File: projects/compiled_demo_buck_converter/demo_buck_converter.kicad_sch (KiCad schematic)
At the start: 7 parts, among them U1 LM2596-5

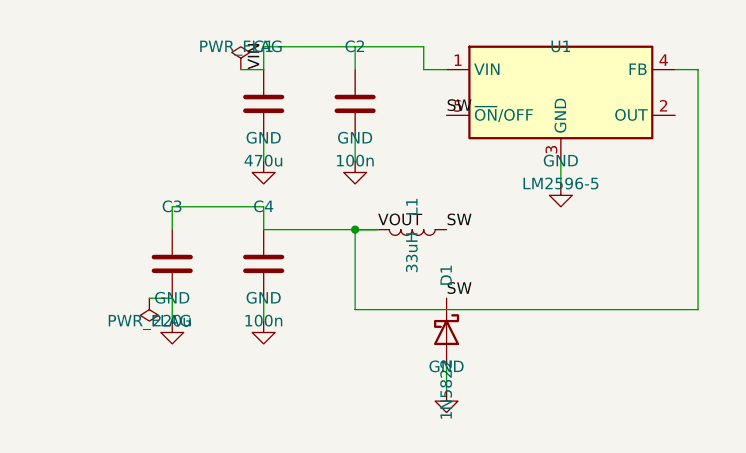
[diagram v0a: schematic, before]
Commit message: F3d+F3e: multi-unit parts and the textplace field autoplacer
Multi-unit: one Symbol per unit (shared ref+lib, distinct unit); nets and
anchors qualify pins as "REF.unit.pin". Resolver targets a specific placed
unit; the geometry probe instantiates per unit. NE5532 (units A/B/C)
compiles first try with both feedback loops wired.

textplace (internal/place2/textplace): deterministic text autoplacement run
at the end of compilation — every visible Reference/Value block is re-placed
horizontally at the least-overlapping side of its body, colliding net labels
flip around their anchor. Fixes the text-collision family the user flagged
on the buck render. KiCad gotcha baked into the pass: a field's drawn angle
is field+symbol rotation, so fields on 90/270 symbols carry a compensating
90 to display horizontal.

All 7 reference circuits now compile from declarative sources with clean
text. Gate demotions (buck SW, ne555 THR/DISCH) are by-design label
fallbacks, zero geometry violations everywhere.

Co-Authored-By: Claude Fable 5 <noreply@anthropic.com>
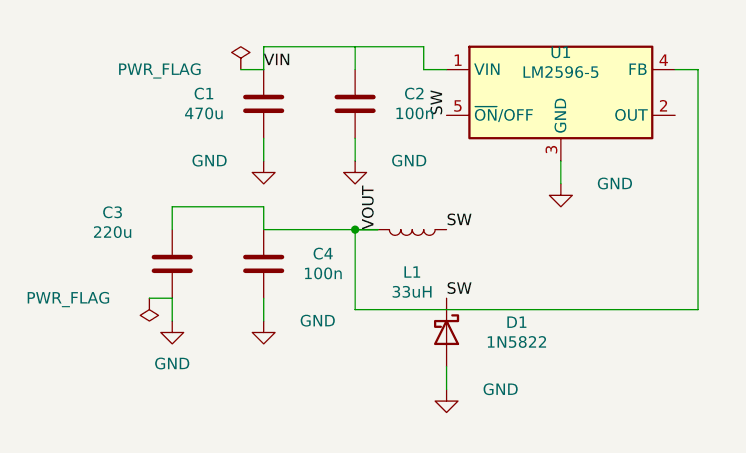
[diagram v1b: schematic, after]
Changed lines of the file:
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@@
     (at 71.12 27.94 0) (unit 1) (exclude_from_sim no) (in_bom yes) (on_board yes) (dnp no)
     (property "Reference" "U1"
-      (at 71.12 22.86 0)
+      (at 71.12 23.52 0)
       (effects
         (font (size 1.27 1.27))))
     (property "Value" "LM2596-5"
-      (at 71.12 38.1 0)
+      (at 71.12 25.72 0)
       (effects
         (font (size 1.27 1.27))))
@@
     (instances
       (project ""
-        (path "/991c5326-0a93-4272-96e1-b9ad8c3713b2" (reference "U1") (unit 1)))))
+        (path "/108c6312-12e9-447c-9139-bc7fdfa02d10" (reference "U1") (unit 1)))))
   (symbol (lib_id "Device:C")
     (at 48.26 29.21 0) (unit 1) (exclude_from_sim no) (in_bom yes) (on_board yes) (dnp no)
     (property "Reference" "C2"
-      (at 48.26 22.86 0)
+      (at 54.87 28.11 0)
       (effects
         (font (size 1.27 1.27))))
     (property "Value" "100n"
-      (at 48.26 35.56 0)
+      (at 54.87 30.31 0)
       (effects
         (font (size 1.27 1.27))))
@@
     (instances
       (project ""
-        (path "/991c5326-0a93-4272-96e1-b9ad8c3713b2" (reference "C2") (unit 1)))))
+        (path "/108c6312-12e9-447c-9139-bc7fdfa02d10" (reference "C2") (unit 1)))))
   (symbol (lib_id "Device:C")
     (at 38.1 29.21 0) (unit 1) (exclude_from_sim no) (in_bom yes) (on_board yes) (dnp no)
     (property "Reference" "C1"
-      (at 38.1 22.86 0)
+      (at 31.49 28.11 0)
       (effects
         (font (size 1.27 1.27))))
     (property "Value" "470u"
-      (at 38.1 35.56 0)
+      (at 31.49 30.31 0)
       (effects
         (font (size 1.27 1.27))))
@@
     (instances
       (project ""
-        (path "/991c5326-0a93-4272-96e1-b9ad8c3713b2" (reference "C1") (unit 1)))))
+        (path "/108c6312-12e9-447c-9139-bc7fdfa02d10" (reference "C1") (unit 1)))))
   (symbol (lib_id "Device:L")
     (at 54.61 43.18 270) (unit 1) (exclude_from_sim no) (in_bom yes) (on_board yes) (dnp no)
     (property "Reference" "L1"
-      (at 54.61 40.64 0)
+      (at 54.61 47.94 90)
       (effects
         (font (size 1.27 1.27))))
     (property "Value" "33uH"
-      (at 54.61 45.72 0)
+      (at 54.61 50.14 90)
       (effects
         (font (size 1.27 1.27))))
@@
     (instances
       (project ""
-        (path "/991c5326-0a93-4272-96e1-b9ad8c3713b2" (reference "L1") (unit 1)))))
+        (path "/108c6312-12e9-447c-9139-bc7fdfa02d10" (reference "L1") (unit 1)))))
   (symbol (lib_id "Diode:1N5822")
     (at 58.42 54.61 270) (unit 1) (exclude_from_sim no) (in_bom yes) (on_board yes) (dnp no)
     (property "Reference" "D1"
-      (at 58.42 48.26 0)
+      (at 66.23 53.51 90)
       (effects
         (font (size 1.27 1.27))))
     (property "Value" "1N5822"
-      (at 58.42 60.96 0)
+      (at 66.23 55.71 90)
       (effects
         (font (size 1.27 1.27))))
@@
     (instances
       (project ""
-        (path "/991c5326-0a93-4272-96e1-b9ad8c3713b2" (reference "D1") (unit 1)))))
+        (path "/108c6312-12e9-447c-9139-bc7fdfa02d10" (reference "D1") (unit 1)))))
   (symbol (lib_id "Device:C")
     (at 38.1 46.99 0) (unit 1) (exclude_from_sim no) (in_bom yes) (on_board yes) (dnp no)
     (property "Reference" "C4"
-      (at 38.1 40.64 0)
+      (at 44.71 45.89 0)
       (effects
         (font (size 1.27 1.27))))
     (property "Value" "100n"
-      (at 38.1 53.34 0)
+      (at 44.71 48.09 0)
       (effects
         (font (size 1.27 1.27))))
@@
     (instances
       (project ""
-        (path "/991c5326-0a93-4272-96e1-b9ad8c3713b2" (reference "C4") (unit 1)))))
+        (path "/108c6312-12e9-447c-9139-bc7fdfa02d10" (reference "C4") (unit 1)))))
   (symbol (lib_id "Device:C")
     (at 27.94 46.99 0) (unit 1) (exclude_from_sim no) (in_bom yes) (on_board yes) (dnp no)
     (property "Reference" "C3"
-      (at 27.94 40.64 0)
+      (at 21.33 41.3 0)
       (effects
         (font (size 1.27 1.27))))
     (property "Value" "220u"
-      (at 27.94 53.34 0)
+      (at 21.33 43.5 0)
       (effects
         (font (size 1.27 1.27))))
@@
     (instances
       (project ""
-        (path "/991c5326-0a93-4272-96e1-b9ad8c3713b2" (reference "C3") (unit 1)))))
+        (path "/108c6312-12e9-447c-9139-bc7fdfa02d10" (reference "C3") (unit 1)))))
   (symbol (lib_id "power:GND")
     (at 71.12 38.1 0) (unit 1) (exclude_from_sim no) (in_bom no) (on_board no) (dnp no)
@@
         (font (size 1.27 1.27)) (hide yes)))
     (property "Value" "GND"
-      (at 71.12 35.56 0)
+      (at 77.13 38.1 0)
       (effects
         (font (size 1.27 1.27))))
@@
     (instances
       (project ""
-        (path "/991c5326-0a93-4272-96e1-b9ad8c3713b2" (reference "#PWR01") (unit 1)))))
+        (path "/108c6312-12e9-447c-9139-bc7fdfa02d10" (reference "#PWR01") (unit 1)))))
   (wire
     (pts (xy 71.12 35.56) (xy 71.12 38.1))
@@
         (font (size 1.27 1.27)) (hide yes)))
     (property "Value" "GND"
-      (at 38.1 33.02 0)
+      (at 32.09 35.56 0)
       (effects
         (font (size 1.27 1.27))))
@@
     (instances
       (project ""
-        (path "/991c5326-0a93-4272-96e1-b9ad8c3713b2" (reference "#PWR02") (unit 1)))))
+        (path "/108c6312-12e9-447c-9139-bc7fdfa02d10" (reference "#PWR02") (unit 1)))))
   (wire
     (pts (xy 38.1 33.02) (xy 38.1 35.56))
@@
         (font (size 1.27 1.27)) (hide yes)))
     (property "Value" "GND"
-      (at 48.26 33.02 0)
+      (at 54.27 35.56 0)
       (effects
         (font (size 1.27 1.27))))
@@
     (instances
       (project ""
-        (path "/991c5326-0a93-4272-96e1-b9ad8c3713b2" (reference "#PWR03") (unit 1)))))
+        (path "/108c6312-12e9-447c-9139-bc7fdfa02d10" (reference "#PWR03") (unit 1)))))
   (wire
     (pts (xy 48.26 33.02) (xy 48.26 35.56))
@@
         (font (size 1.27 1.27)) (hide yes)))
     (property "Value" "GND"
-      (at 27.94 50.8 0)
+      (at 27.94 58.1 0)
       (effects
         (font (size 1.27 1.27))))
@@
     (instances
       (project ""
-        (path "/991c5326-0a93-4272-96e1-b9ad8c3713b2" (reference "#PWR04") (unit 1)))))
+        (path "/108c6312-12e9-447c-9139-bc7fdfa02d10" (reference "#PWR04") (unit 1)))))
   (wire
     (pts (xy 27.94 50.8) (xy 27.94 53.34))
@@
         (font (size 1.27 1.27)) (hide yes)))
     (property "Value" "GND"
-      (at 38.1 50.8 0)
+      (at 44.11 53.34 0)
       (effects
         (font (size 1.27 1.27))))
@@
     (instances
       (project ""
-        (path "/991c5326-0a93-4272-96e1-b9ad8c3713b2" (reference "#PWR05") (unit 1)))))
+        (path "/108c6312-12e9-447c-9139-bc7fdfa02d10" (reference "#PWR05") (unit 1)))))
   (wire
     (pts (xy 38.1 50.8) (xy 38.1 53.34))
@@
         (font (size 1.27 1.27)) (hide yes)))
     (property "Value" "GND"
-      (at 58.42 58.42 0)
+      (at 64.43 60.96 0)
       (effects
         (font (size 1.27 1.27))))
@@
     (instances
       (project ""
-        (path "/991c5326-0a93-4272-96e1-b9ad8c3713b2" (reference "#PWR06") (unit 1)))))
+        (path "/108c6312-12e9-447c-9139-bc7fdfa02d10" (reference "#PWR06") (unit 1)))))
   (wire
     (pts (xy 58.42 58.42) (xy 58.42 60.96))
@@
     (stroke (width 0) (type default)))
   (label "VIN"
-    (at 38.1 25.4 90) (fields_autoplaced yes)
+    (at 38.1 25.4 0) (fields_autoplaced yes)
     (effects
       (font (size 1.27 1.27)) (justify left bottom))
@@
     (color 0 0 0 0))
   (label "VOUT"
-    (at 50.8 43.18 180) (fields_autoplaced yes)
+    (at 50.8 43.18 270) (fields_autoplaced yes)
     (effects
       (font (size 1.27 1.27)) (justify left bottom))
@@
         (font (size 1.27 1.27)) (hide yes))))
   (label "SW"
-    (at 58.42 30.48 0) (fields_autoplaced yes)
+    (at 58.42 30.48 270) (fields_autoplaced yes)
     (effects
       (font (size 1.27 1.27)) (justify left bottom))
@@
         (font (size 1.27 1.27)) (hide yes)))
     (property "Value" "PWR_FLAG"
-      (at 25.4 53.34 0)
+      (at 16.39 50.8 0)
       (effects
         (font (size 1.27 1.27))))
@@
     (instances
       (project ""
-        (path "/991c5326-0a93-4272-96e1-b9ad8c3713b2" (reference "#FLG01") (unit 1)))))
+        (path "/108c6312-12e9-447c-9139-bc7fdfa02d10" (reference "#FLG01") (unit 1)))))
   (wire
     (pts (xy 27.94 50.8) (xy 25.4 50.8))
@@
         (font (size 1.27 1.27)) (hide yes)))
     (property "Value" "PWR_FLAG"
-      (at 35.56 22.86 0)
+      (at 26.55 25.4 0)
       (effects
         (font (size 1.27 1.27))))
@@
     (instances
       (project ""
-        (path "/991c5326-0a93-4272-96e1-b9ad8c3713b2" (reference "#FLG02") (unit 1)))))
+        (path "/108c6312-12e9-447c-9139-bc7fdfa02d10" (reference "#FLG02") (unit 1)))))
   (wire
     (pts (xy 38.1 25.4) (xy 35.56 25.4))

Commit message: F5: human-quality pass — weld, route beauty, silent flags, design guide
The user's mandate: schematics must read as hand-drawn — tidy wires over
tag pairs, clean corners, nothing on screen but symbol, model and value.

- internal/place2/weld: same-net label islands get welded into real wires
  (straight/L/Z) whenever a clean corridor exists; every candidate is
  validated against gate.Check and reverted on any new violation. Redundant
  labels removed, one kept as documentation.
- routeNets beauty policy: a path with more than 3 bends or >70% detour
  over Manhattan distance reads worse than a label — demoted before it is
  ever drawn. Combined with weld this replaces snakes with short wires.
- PWR_FLAG value text hidden (sexp.HidePropertyText): the flag exists for
  ERC, not for the reader.
- design_guide: human-schematic conventions (signal flow, wire-vs-label,
  spacing recipes in grid cells, iteration protocol) distilled from
  SparkFun/KLC/IEEE-315/Altium/H&H research, embedded in the binary and
  served as an MCP tool for authoring LLMs.
- Crystal clusters reworked in both MCU sources: vertical crystal, straight
  XTAL1, single-L XTAL2, horizontal load caps — full Pierce oscillator
  wiring, zero label pairs. NE555 timing chain now fully wired via weld.

Co-Authored-By: Claude Fable 5 <noreply@anthropic.com>
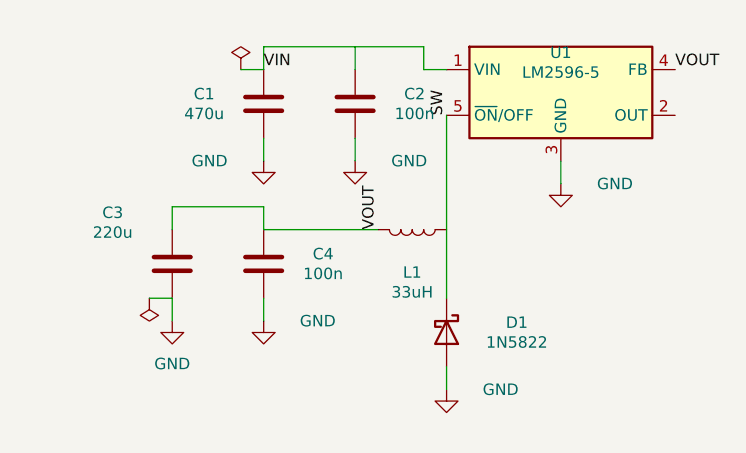
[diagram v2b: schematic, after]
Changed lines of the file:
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@@
     (instances
       (project ""
-        (path "/108c6312-12e9-447c-9139-bc7fdfa02d10" (reference "U1") (unit 1)))))
+        (path "/758c67ba-c1c8-4ce3-ab23-cb495e0d4090" (reference "U1") (unit 1)))))
   (symbol (lib_id "Device:C")
     (at 48.26 29.21 0) (unit 1) (exclude_from_sim no) (in_bom yes) (on_board yes) (dnp no)
@@
     (instances
       (project ""
-        (path "/108c6312-12e9-447c-9139-bc7fdfa02d10" (reference "C2") (unit 1)))))
+        (path "/758c67ba-c1c8-4ce3-ab23-cb495e0d4090" (reference "C2") (unit 1)))))
   (symbol (lib_id "Device:C")
     (at 38.1 29.21 0) (unit 1) (exclude_from_sim no) (in_bom yes) (on_board yes) (dnp no)
@@
     (instances
       (project ""
-        (path "/108c6312-12e9-447c-9139-bc7fdfa02d10" (reference "C1") (unit 1)))))
+        (path "/758c67ba-c1c8-4ce3-ab23-cb495e0d4090" (reference "C1") (unit 1)))))
   (symbol (lib_id "Device:L")
     (at 54.61 43.18 270) (unit 1) (exclude_from_sim no) (in_bom yes) (on_board yes) (dnp no)
@@
     (instances
       (project ""
-        (path "/108c6312-12e9-447c-9139-bc7fdfa02d10" (reference "L1") (unit 1)))))
+        (path "/758c67ba-c1c8-4ce3-ab23-cb495e0d4090" (reference "L1") (unit 1)))))
   (symbol (lib_id "Diode:1N5822")
     (at 58.42 54.61 270) (unit 1) (exclude_from_sim no) (in_bom yes) (on_board yes) (dnp no)
@@
     (instances
       (project ""
-        (path "/108c6312-12e9-447c-9139-bc7fdfa02d10" (reference "D1") (unit 1)))))
+        (path "/758c67ba-c1c8-4ce3-ab23-cb495e0d4090" (reference "D1") (unit 1)))))
   (symbol (lib_id "Device:C")
     (at 38.1 46.99 0) (unit 1) (exclude_from_sim no) (in_bom yes) (on_board yes) (dnp no)
@@
     (instances
       (project ""
-        (path "/108c6312-12e9-447c-9139-bc7fdfa02d10" (reference "C4") (unit 1)))))
+        (path "/758c67ba-c1c8-4ce3-ab23-cb495e0d4090" (reference "C4") (unit 1)))))
   (symbol (lib_id "Device:C")
     (at 27.94 46.99 0) (unit 1) (exclude_from_sim no) (in_bom yes) (on_board yes) (dnp no)
@@
     (instances
       (project ""
-        (path "/108c6312-12e9-447c-9139-bc7fdfa02d10" (reference "C3") (unit 1)))))
+        (path "/758c67ba-c1c8-4ce3-ab23-cb495e0d4090" (reference "C3") (unit 1)))))
   (symbol (lib_id "power:GND")
     (at 71.12 38.1 0) (unit 1) (exclude_from_sim no) (in_bom no) (on_board no) (dnp no)
@@
     (instances
       (project ""
-        (path "/108c6312-12e9-447c-9139-bc7fdfa02d10" (reference "#PWR01") (unit 1)))))
+        (path "/758c67ba-c1c8-4ce3-ab23-cb495e0d4090" (reference "#PWR01") (unit 1)))))
   (wire
     (pts (xy 71.12 35.56) (xy 71.12 38.1))
@@
     (instances
       (project ""
-        (path "/108c6312-12e9-447c-9139-bc7fdfa02d10" (reference "#PWR02") (unit 1)))))
+        (path "/758c67ba-c1c8-4ce3-ab23-cb495e0d4090" (reference "#PWR02") (unit 1)))))
   (wire
     (pts (xy 38.1 33.02) (xy 38.1 35.56))
@@
     (instances
       (project ""
-        (path "/108c6312-12e9-447c-9139-bc7fdfa02d10" (reference "#PWR03") (unit 1)))))
+        (path "/758c67ba-c1c8-4ce3-ab23-cb495e0d4090" (reference "#PWR03") (unit 1)))))
   (wire
     (pts (xy 48.26 33.02) (xy 48.26 35.56))
@@
     (instances
       (project ""
-        (path "/108c6312-12e9-447c-9139-bc7fdfa02d10" (reference "#PWR04") (unit 1)))))
+        (path "/758c67ba-c1c8-4ce3-ab23-cb495e0d4090" (reference "#PWR04") (unit 1)))))
   (wire
     (pts (xy 27.94 50.8) (xy 27.94 53.34))
@@
     (instances
       (project ""
-        (path "/108c6312-12e9-447c-9139-bc7fdfa02d10" (reference "#PWR05") (unit 1)))))
+        (path "/758c67ba-c1c8-4ce3-ab23-cb495e0d4090" (reference "#PWR05") (unit 1)))))
   (wire
     (pts (xy 38.1 50.8) (xy 38.1 53.34))
@@
     (instances
       (project ""
-        (path "/108c6312-12e9-447c-9139-bc7fdfa02d10" (reference "#PWR06") (unit 1)))))
+        (path "/758c67ba-c1c8-4ce3-ab23-cb495e0d4090" (reference "#PWR06") (unit 1)))))
   (wire
     (pts (xy 58.42 58.42) (xy 58.42 60.96))
@@
     (pts (xy 27.94 40.64) (xy 27.94 43.18))
     (stroke (width 0) (type default)))
-  (wire
-    (pts (xy 50.8 43.18) (xy 48.26 43.18))
-    (stroke (width 0) (type default)))
-  (wire
-    (pts (xy 48.26 43.18) (xy 48.26 52.07))
-    (stroke (width 0) (type default)))
-  (wire
-    (pts (xy 48.26 52.07) (xy 86.36 52.07))
-    (stroke (width 0) (type default)))
-  (wire
-    (pts (xy 86.36 52.07) (xy 86.36 25.4))
-    (stroke (width 0) (type default)))
-  (wire
-    (pts (xy 86.36 25.4) (xy 83.82 25.4))
-    (stroke (width 0) (type default)))
-  (junction (at 48.26 43.18) (diameter 0)
-    (color 0 0 0 0))
   (label "VOUT"
     (at 50.8 43.18 270) (fields_autoplaced yes)
@@
       (effects
         (font (size 1.27 1.27)) (hide yes))))
-  (label "SW"
-    (at 58.42 30.48 270) (fields_autoplaced yes)
+  (label "VOUT"
+    (at 83.82 25.4 0) (fields_autoplaced yes)
     (effects
       (font (size 1.27 1.27)) (justify left bottom))
@@
         (font (size 1.27 1.27)) (hide yes))))
   (label "SW"
-    (at 58.42 43.18 0) (fields_autoplaced yes)
+    (at 58.42 30.48 90) (fields_autoplaced yes)
     (effects
       (font (size 1.27 1.27)) (justify left bottom))
@@
       (effects
         (font (size 1.27 1.27)) (hide yes))))
-  (label "SW"
-    (at 58.42 50.8 0) (fields_autoplaced yes)
-    (effects
-      (font (size 1.27 1.27)) (justify left bottom))
-    (property "Intersheet References" ""
-      (at 0 0 0)
-      (effects
-        (font (size 1.27 1.27)) (hide yes))))
+  (wire
+    (pts (xy 58.42 43.18) (xy 58.42 50.8))
+    (stroke (width 0) (type default)))
+  (wire
+    (pts (xy 58.42 30.48) (xy 58.42 43.18))
+    (stroke (width 0) (type default)))
   (symbol (lib_id "power:PWR_FLAG")
     (at 25.4 50.8 180) (unit 1) (exclude_from_sim no) (in_bom no) (on_board no) (dnp no)
@@
         (font (size 1.27 1.27)) (hide yes)))
     (property "Value" "PWR_FLAG"
-      (at 16.39 50.8 0)
-      (effects
-        (font (size 1.27 1.27))))
+      (at 25.4 53.34 0)
+      (effects
+        (font (size 1.27 1.27)) (hide yes)))
     (property "Footprint" ""
       (at 25.4 50.8 0)
@@
     (instances
       (project ""
-        (path "/108c6312-12e9-447c-9139-bc7fdfa02d10" (reference "#FLG01") (unit 1)))))
+        (path "/758c67ba-c1c8-4ce3-ab23-cb495e0d4090" (reference "#FLG01") (unit 1)))))
   (wire
     (pts (xy 27.94 50.8) (xy 25.4 50.8))
@@
         (font (size 1.27 1.27)) (hide yes)))
     (property "Value" "PWR_FLAG"
-      (at 26.55 25.4 0)
-      (effects
-        (font (size 1.27 1.27))))
+      (at 35.56 22.86 0)
+      (effects
+        (font (size 1.27 1.27)) (hide yes)))
     (property "Footprint" ""
       (at 35.56 25.4 0)
@@
     (instances
       (project ""
-        (path "/108c6312-12e9-447c-9139-bc7fdfa02d10" (reference "#FLG02") (unit 1)))))
+        (path "/758c67ba-c1c8-4ce3-ab23-cb495e0d4090" (reference "#FLG02") (unit 1)))))
   (wire
     (pts (xy 38.1 25.4) (xy 35.56 25.4))

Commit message: Body model sees real symbol graphics; quiet nets drop junction tags
User-reported flaws from visual review, both fixed at the root:

- Wires over symbol artwork: the body model was pin-derived and blind to
  drawn graphics — an op-amp triangle's vertices stick out beyond the pin
  box, so "legal" wires crossed the drawing. internal/sexp/graphics.go now
  parses rectangle/polyline/circle/arc/bezier extents per unit with the
  exact pin transform; metrics.BodyBBox unions them with the legacy box,
  clamped off pin tips (Device:LED's emission arrows overhang the cathode
  pin and would have swallowed it). NE5532 feedback: 8 stroke crossings
  through the triangle before, 0 after (loops now label pairs). The model
  also exposed genuinely bad baked geometry in mcu_minimal_atmega328's
  crystal — repositioned with the template contract intact.

- "ANODE" tag on a resistor leg: net names with a "_" prefix are now
  quiet — connectivity only, their documentation label is stripped at the
  end of compilation when the wiring alone keeps the net whole. Junction
  nodes (R->LED) stay unlabeled like in any hand-drawn schematic.

- Battery hump: led_18650 anchors R1 in the pin's exit direction; the
  design guide gains the "respect the pin's exit direction" and "internal
  junctions carry no tag" recipes.

Co-Authored-By: Claude Fable 5 <noreply@anthropic.com>
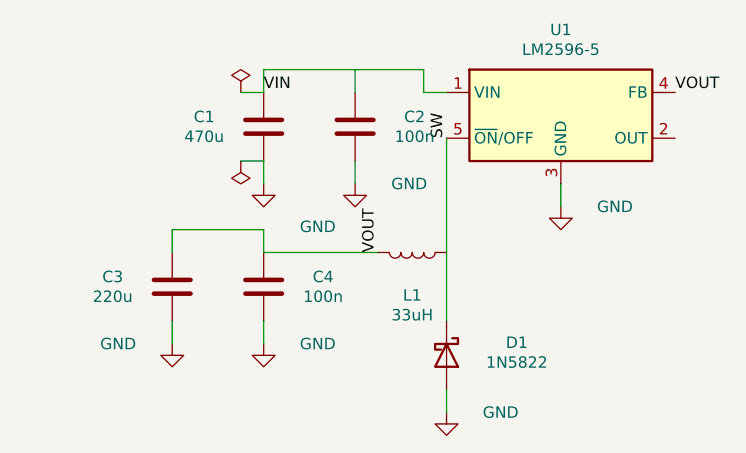
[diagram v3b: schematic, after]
